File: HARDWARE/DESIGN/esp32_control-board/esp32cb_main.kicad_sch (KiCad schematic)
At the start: 25 parts, among them J204 USB-prog, SW201 Boot, SW202 Reset, U203 ESP32-S3-WROOM-1U, U204 USBLC6-2SC6

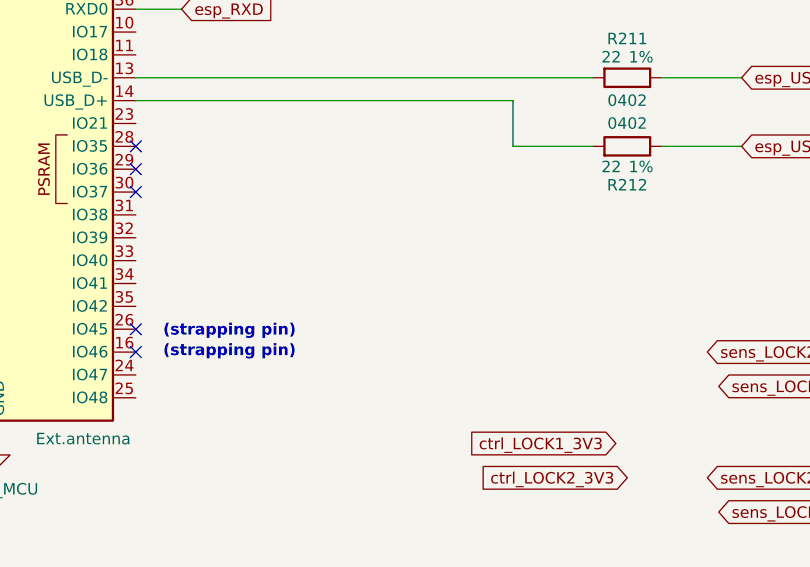
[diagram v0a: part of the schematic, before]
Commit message: 60905 - fuse-holder replaced, led-strip connector added
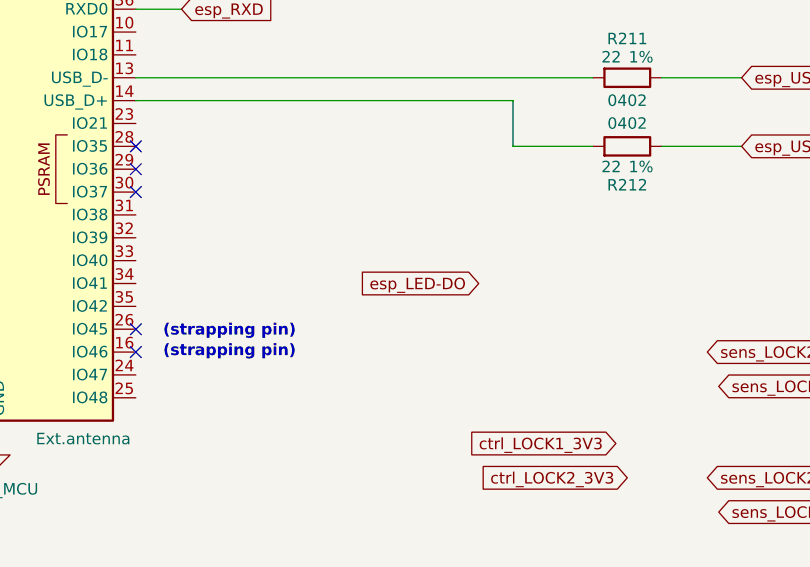
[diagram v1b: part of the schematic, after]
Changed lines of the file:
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@@
+		)
+	)
+	(global_label "esp_LED-DO"
+		(shape input)
+		(at 214.63 120.65 180)
+		(fields_autoplaced yes)
+		(effects
+			(font
+				(size 1.27 1.27)
+			)
+			(justify right)
+		)
+		(property "Intersheetrefs" "${INTERSHEET_REFS}"
+			(at 199.7915 120.65 0)
+			(hide yes)
+			(show_name no)
+			(do_not_autoplace no)
+			(effects
+				(font
+					(size 1.27 1.27)
+				)
+				(justify right)
+			)
 		)
 	)

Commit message: 60908 - PCB-layout updated
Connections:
- net ai_BatteryVoltage: now also U203.38 (IO2)
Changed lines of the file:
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@@
 	(global_label "esp_LED-DO"
 		(shape input)
-		(at 214.63 120.65 180)
-		(fields_autoplaced yes)
-		(effects
-			(font
-				(size 1.27 1.27)
-			)
-			(justify right)
-		)
-		(property "Intersheetrefs" "${INTERSHEET_REFS}"
-			(at 199.7915 120.65 0)
+		(at 125.73 147.32 180)
+		(fields_autoplaced yes)
+		(effects
+			(font
+				(size 1.27 1.27)
+			)
+			(justify right)
+		)
+		(property "Intersheetrefs" "${INTERSHEET_REFS}"
+			(at 110.8915 147.32 0)
 			(hide yes)
 			(show_name no)
@@
 				)
 				(justify left)
+			)
+		)
+	)
+	(global_label "ai_BatteryVoltage"
+		(shape input)
+		(at 146.05 97.79 180)
+		(fields_autoplaced yes)
+		(effects
+			(font
+				(size 1.27 1.27)
+			)
+			(justify right)
+		)
+		(property "Intersheetrefs" "${INTERSHEET_REFS}"
+			(at 126.6155 97.79 0)
+			(hide yes)
+			(show_name no)
+			(do_not_autoplace no)
+			(effects
+				(font
+					(size 1.27 1.27)
+				)
+				(justify right)
 			)
 		)
@@
 					(unit 1)
 				)
+			)
+		)
+	)
+	(symbol
+		(lib_id "power:+5VP")
+		(at 104.14 207.01 0)
+		(unit 1)
+		(body_style 1)
+		(exclude_from_sim no)
+		(in_bom yes)
+		(on_board yes)
+		(in_pos_files yes)
+		(dnp no)
+		(property "Reference" "#PWR0134"
+			(at 104.14 210.82 0)
+			(hide yes)
+			(show_name no)
+			(do_not_autoplace no)
+			(effects
+				(font
+					(size 1.27 1.27)
+				)
+			)
+		)
+		(property "Value" "Vusb"
+			(at 104.14 202.692 0)
+			(show_name no)
+			(do_not_autoplace no)
+			(effects
+				(font
+					(size 1.27 1.27)
+				)
+			)
+		)
+		(property "Footprint" ""
+			(at 104.14 207.01 0)
+			(hide yes)
+			(show_name no)
+			(do_not_autoplace no)
+			(effects
+				(font
+					(size 1.27 1.27)
+				)
+			)
+		)
+		(property "Datasheet" ""
+			(at 104.14 207.01 0)
+			(hide yes)
+			(show_name no)
+			(do_not_autoplace no)
+			(effects
+				(font
+					(size 1.27 1.27)
+				)
+			)
+		)
+		(property "Description" ""
+			(at 104.14 207.01 0)
+			(show_name no)
+			(do_not_autoplace no)
+			(effects
+				(font
+					(size 1.27 1.27)
+				)
+			)
+		)
+		(pin "1"
+		)
+		(instances
+			(project "esp32_control-board"
+				(path "/71812bfc-9597-4f26-a67f-4f6ff697416c/b211aa99-c245-41c6-9b64-a229e59ffb83"
+					(reference "#PWR0134")
+					(unit 1)
+				)

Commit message: 60911 - PCB-layout updated
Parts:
- removed D201: MCU ok, LED_SMD:LED_0603_1608Metric, symbol Device:LED
- added R216: 1k, Resistor_SMD:R_0603_1608Metric, symbol Device:R
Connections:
- net GND_MCU: now also D203.1 (K), D204.1 (K); no longer D202.1 (K)
- net RFID1_irq: now also U203.22 (IO14); no longer U203.9 (IO16)
- net ctrl_LOCK1_3V3: now also U203.9 (IO16)
- net ctrl_LOCK2_3V3: now also U203.11 (IO18)
- net esp_LED-DO: now also R216.2
- net esp_LED_green: no longer R213.1
- net esp_LED_red: now also U203.34 (IO41)
- net esp_TCAN330_ctrl-Shutdown: now also U203.25 (IO48)
- net esp_TCAN330_ctrl-Silent: now also U203.24 (IO47)
- net sens_LOCK1_door_3V3: now also U203.33 (IO40)
- net sens_LOCK1_latch_3V3: now also U203.23 (IO21)
- net sens_LOCK2_door_3V3: now also U203.32 (IO39)
- net sens_LOCK2_latch_3V3: now also U203.31 (IO38)
- net at R214.2: now also D204.2 (A); no longer D202.2 (A)
- net at R213.2: now also D203.2 (A)
- net at U203.10 (IO17): now also R216.1
- net esp_LED_blue: now reaches U203.35 (IO42)
- net esp_LED_blue: now also R213.1
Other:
- moved on the sheet: D203, D204, R213, R214

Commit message: 60911 - Schematic minor update
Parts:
- removed D202: MCU ok, LED_SMD:LED_0603_1608Metric, symbol Device:LED
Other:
- note added: "Indication"
- moved on the sheet: D203, D204, J204, R207, R208, R213, R214, U204
